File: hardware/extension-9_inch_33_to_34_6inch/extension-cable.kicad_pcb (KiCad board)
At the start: 2 copper layers, 32 x 37.1 mm, 4 parts, among them J1 XF2M-3315-1A, U1 ED060XC5

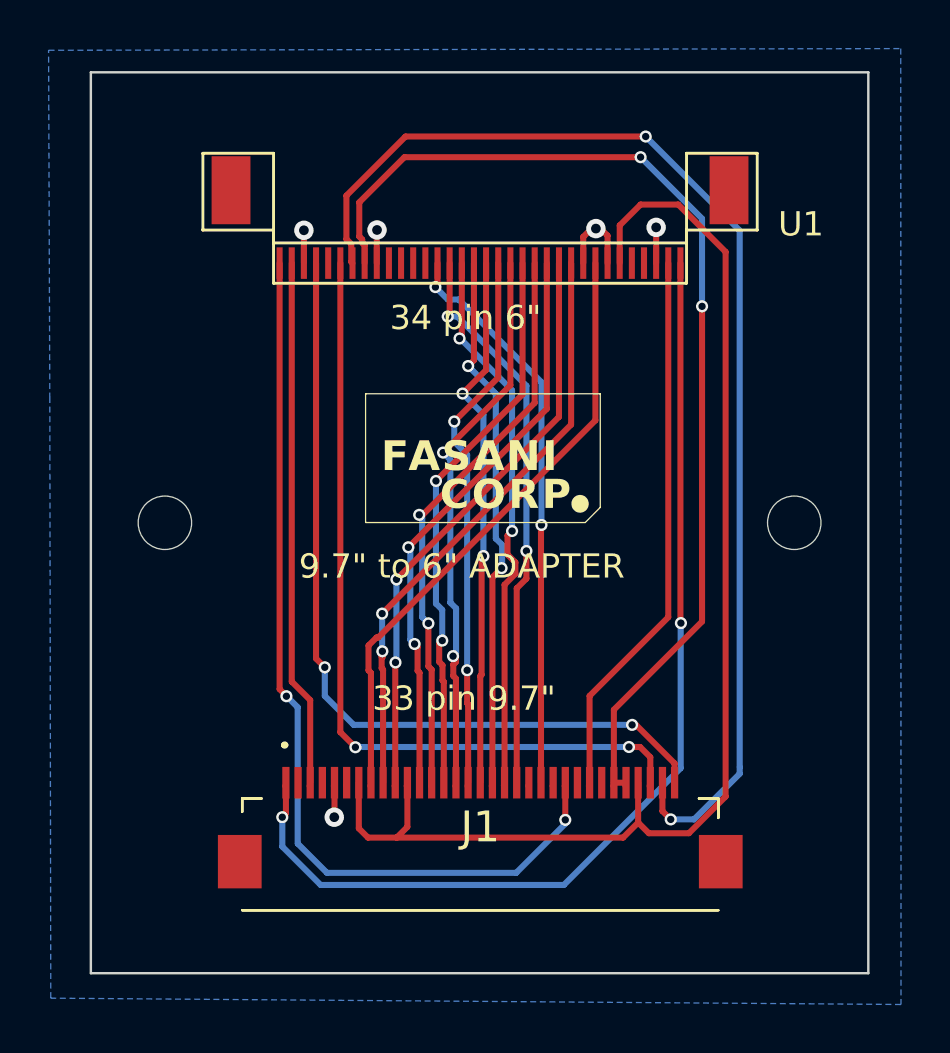
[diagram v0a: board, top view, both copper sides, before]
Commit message: Add double extension cable PCB
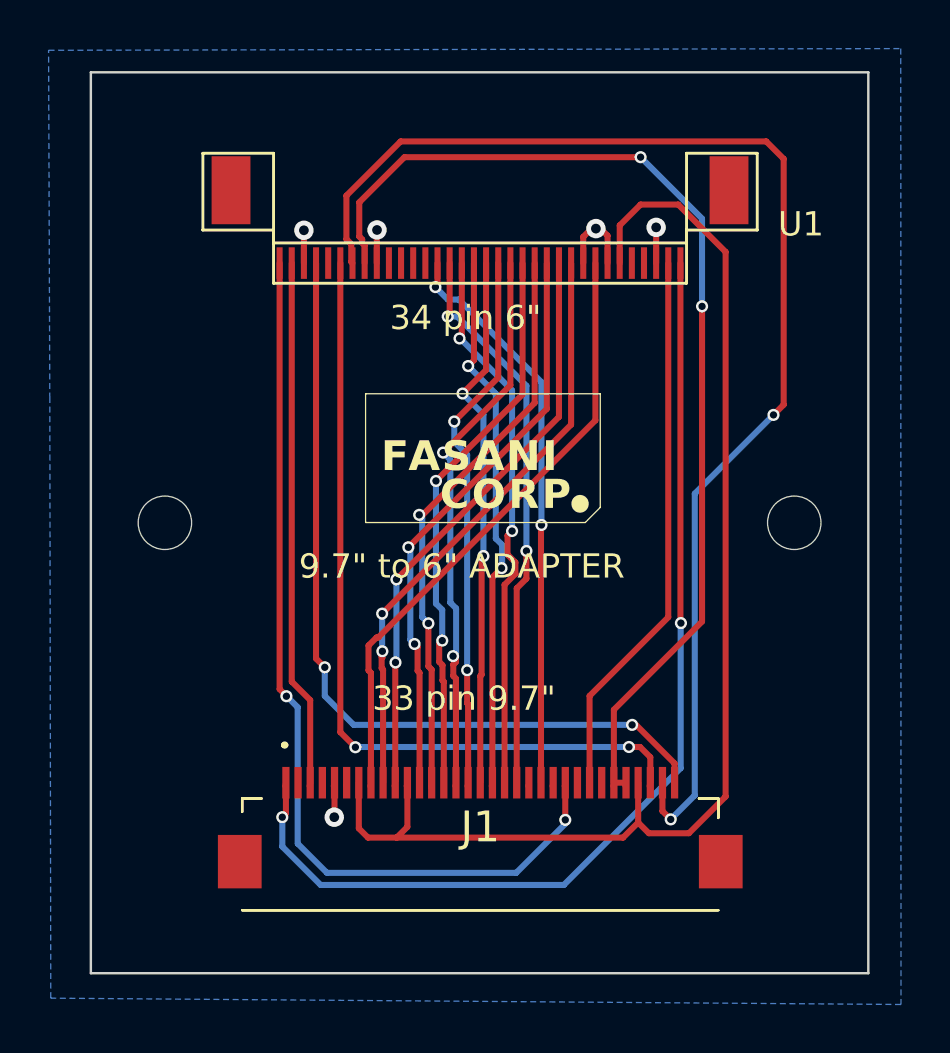
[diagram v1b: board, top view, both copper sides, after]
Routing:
- net /CKV: track 49.3 -> 52.9 mm
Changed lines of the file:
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@@
   (segment (start 88.37 89.24) (end 88.36 89.25) (width 0.25) (layer "B.Cu") (net 28))
   (segment (start 99.62 89.24) (end 88.37 89.24) (width 0.25) (layer "B.Cu") (net 28))
-  (segment (start 88.19 69.27) (end 88.24 69.32) (width 0.25) (layer "F.Cu") (net 29))
-  (segment (start 90.423898 64.11) (end 87.99 66.543898) (width 0.25) (layer "F.Cu") (net 29))
+  (segment (start 105.99 65.03) (end 105.99 75.15) (width 0.25) (layer "F.Cu") (net 29))
   (segment (start 101 91.88) (end 101 90.71) (width 0.25) (layer "F.Cu") (net 29))
-  (segment (start 87.99 66.543898) (end 87.99 68.33538) (width 0.25) (layer "F.Cu") (net 29))
-  (segment (start 88.19 68.53538) (end 88.19 69.27) (width 0.25) (layer "F.Cu") (net 29))
+  (segment (start 88.24 69.32) (end 88.19 69.27) (width 0.25) (layer "F.Cu") (net 29))
   (segment (start 101 91.88) (end 101.34 92.22) (width 0.25) (layer "F.Cu") (net 29))
-  (segment (start 87.99 68.33538) (end 88.19 68.53538) (width 0.25) (layer "F.Cu") (net 29))
-  (segment (start 100.31 64.11) (end 90.423898 64.11) (width 0.25) (layer "F.Cu") (net 29))
+  (segment (start 88.19 69.27) (end 88.19 68.53538) (width 0.25) (layer "F.Cu") (net 29))
+  (segment (start 87.99 68.33538) (end 87.99 66.543898) (width 0.25) (layer "F.Cu") (net 29))
+  (segment (start 105.271949 64.311949) (end 105.99 65.03) (width 0.25) (layer "F.Cu") (net 29))
+  (segment (start 105.99 75.15) (end 105.57 75.57) (width 0.25) (layer "F.Cu") (net 29))
+  (segment (start 88.19 68.53538) (end 87.99 68.33538) (width 0.25) (layer "F.Cu") (net 29))
+  (segment (start 90.221949 64.311949) (end 105.271949 64.311949) (width 0.25) (layer "F.Cu") (net 29))
+  (segment (start 87.99 66.543898) (end 90.221949 64.311949) (width 0.25) (layer "F.Cu") (net 29))
+  (via (at 105.57 75.57) (size 0.5) (drill 0.3) (layers "F.Cu" "B.Cu") (net 29))
   (via (at 101.34 92.22) (size 0.5) (drill 0.3) (layers "F.Cu" "B.Cu") (net 29))
-  (via (at 100.31 64.11) (size 0.5) (drill 0.3) (layers "F.Cu" "B.Cu") (net 29))
-  (segment (start 104.18 90.07) (end 104.18 67.98) (width 0.25) (layer "B.Cu") (net 29))
-  (segment (start 104.18 90.34) (end 102.3 92.22) (width 0.25) (layer "B.Cu") (net 29))
-  (segment (start 104.18 67.98) (end 100.31 64.11) (width 0.25) (layer "B.Cu") (net 29))
-  (segment (start 102.3 92.22) (end 101.34 92.22) (width 0.25) (layer "B.Cu") (net 29))
-  (segment (start 104.18 90.07) (end 104.18 90.34) (width 0.25) (layer "B.Cu") (net 29))
+  (segment (start 102.33 91.23) (end 102.33 78.81) (width 0.25) (layer "B.Cu") (net 29))
+  (segment (start 101.34 92.22) (end 102.33 91.23) (width 0.25) (layer "B.Cu") (net 29))
+  (segment (start 102.33 78.81) (end 105.57 75.57) (width 0.25) (layer "B.Cu") (net 29))
   (segment (start 99.912463 88.33) (end 99.75 88.33) (width 0.25) (layer "F.Cu") (net 30))
   (segment (start 86.74 83.53) (end 86.74 85.6) (width 0.25) (layer "F.Cu") (net 30))

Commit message: Add PCB tester with LEDs & MicroSD
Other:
- rule pad_to_mask_clearance: 0.051 -> 0
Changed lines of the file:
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@@
   )
   (setup
-    (pad_to_mask_clearance 0.051)
-    (solder_mask_min_width 0.25)
+    (pad_to_mask_clearance 0)
     (grid_origin 101.83 84.61)
     (pcbplotparams
@@
     (property "Sheetname" "")
     (property "ki_description" "ED060XC5 E-Paper screen")
-    (attr smd allow_soldermask_bridges)
+    (attr smd)
     (fp_text reference "U1" (at -13.21 1.6) (layer "F.SilkS")
         (effects (font (size 1 1) (thickness 0.15)))
@@
     (property "ki_description" "ED097OC4 9.7\" epaper display")
     (property "ki_keywords" "epaper eink")
-    (attr smd allow_soldermask_bridges)
+    (attr smd)
     (fp_text reference "J1" (at 0 -1.125) (layer "F.SilkS")
         (effects (font (size 1.27 1.27) (thickness 0.254)))
